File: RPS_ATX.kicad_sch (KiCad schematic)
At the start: 35 parts, among them J1 Fan_in, J10 CTRL, J13 Fan_out, J4 17.5V, J5 PS_OUT-, J6 PS_OUT+, J7 RPS_OUT-, J8 MEAS, J9 RPS_OUT+, Q3 AO3400A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

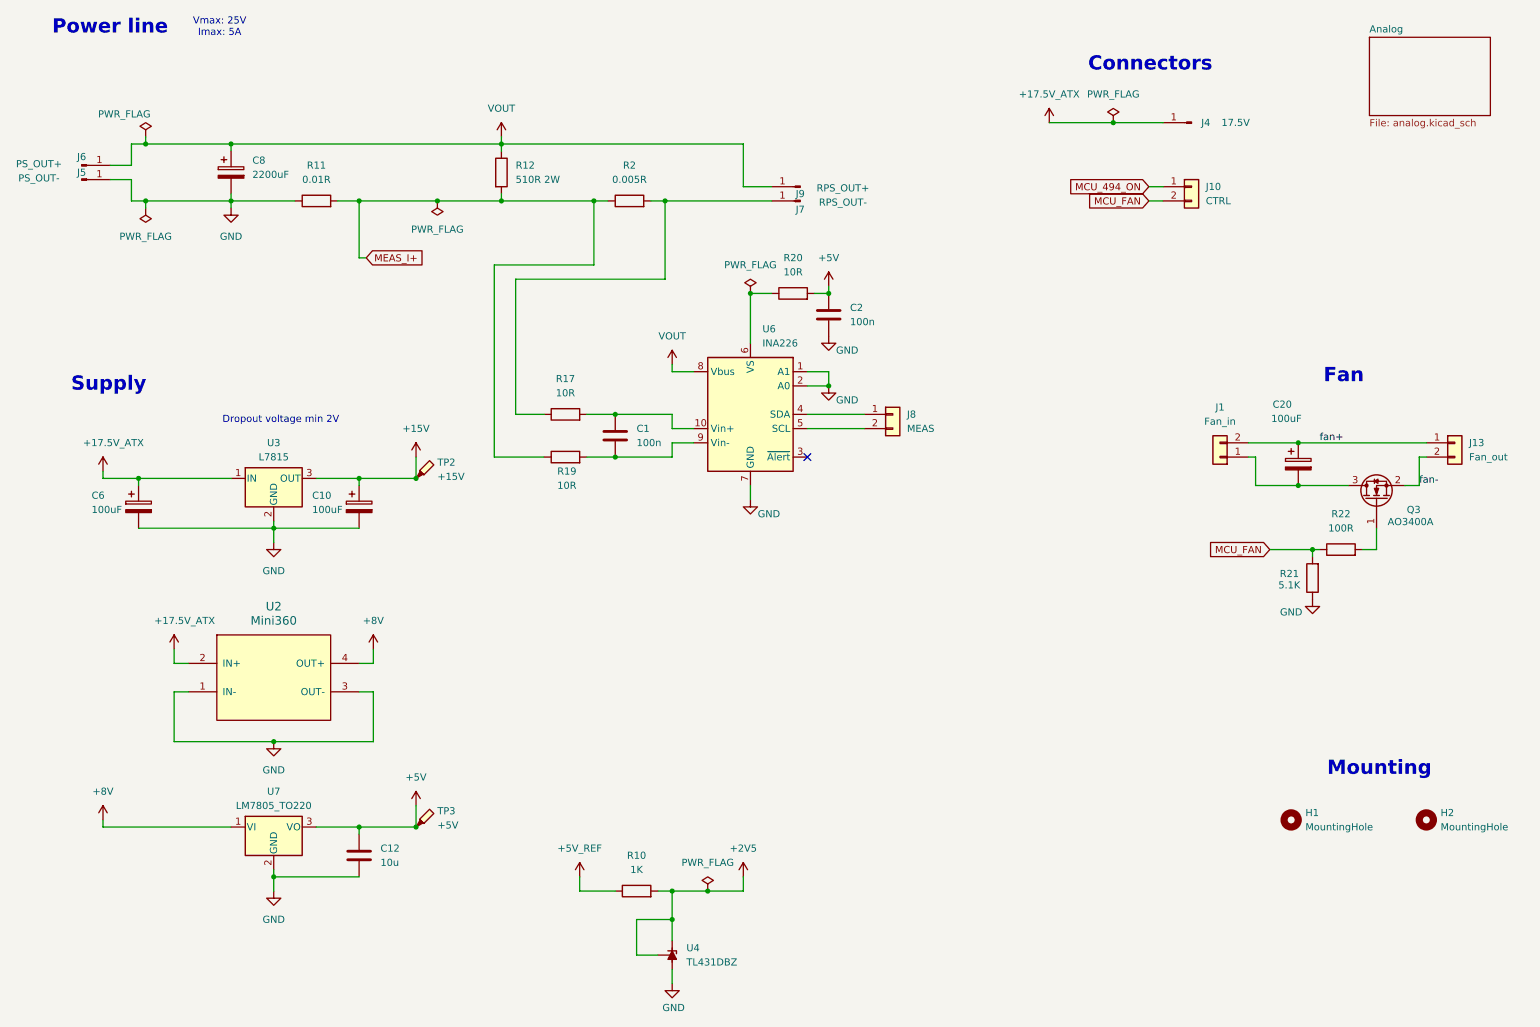
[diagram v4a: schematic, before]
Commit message: lm358 as U and I meas
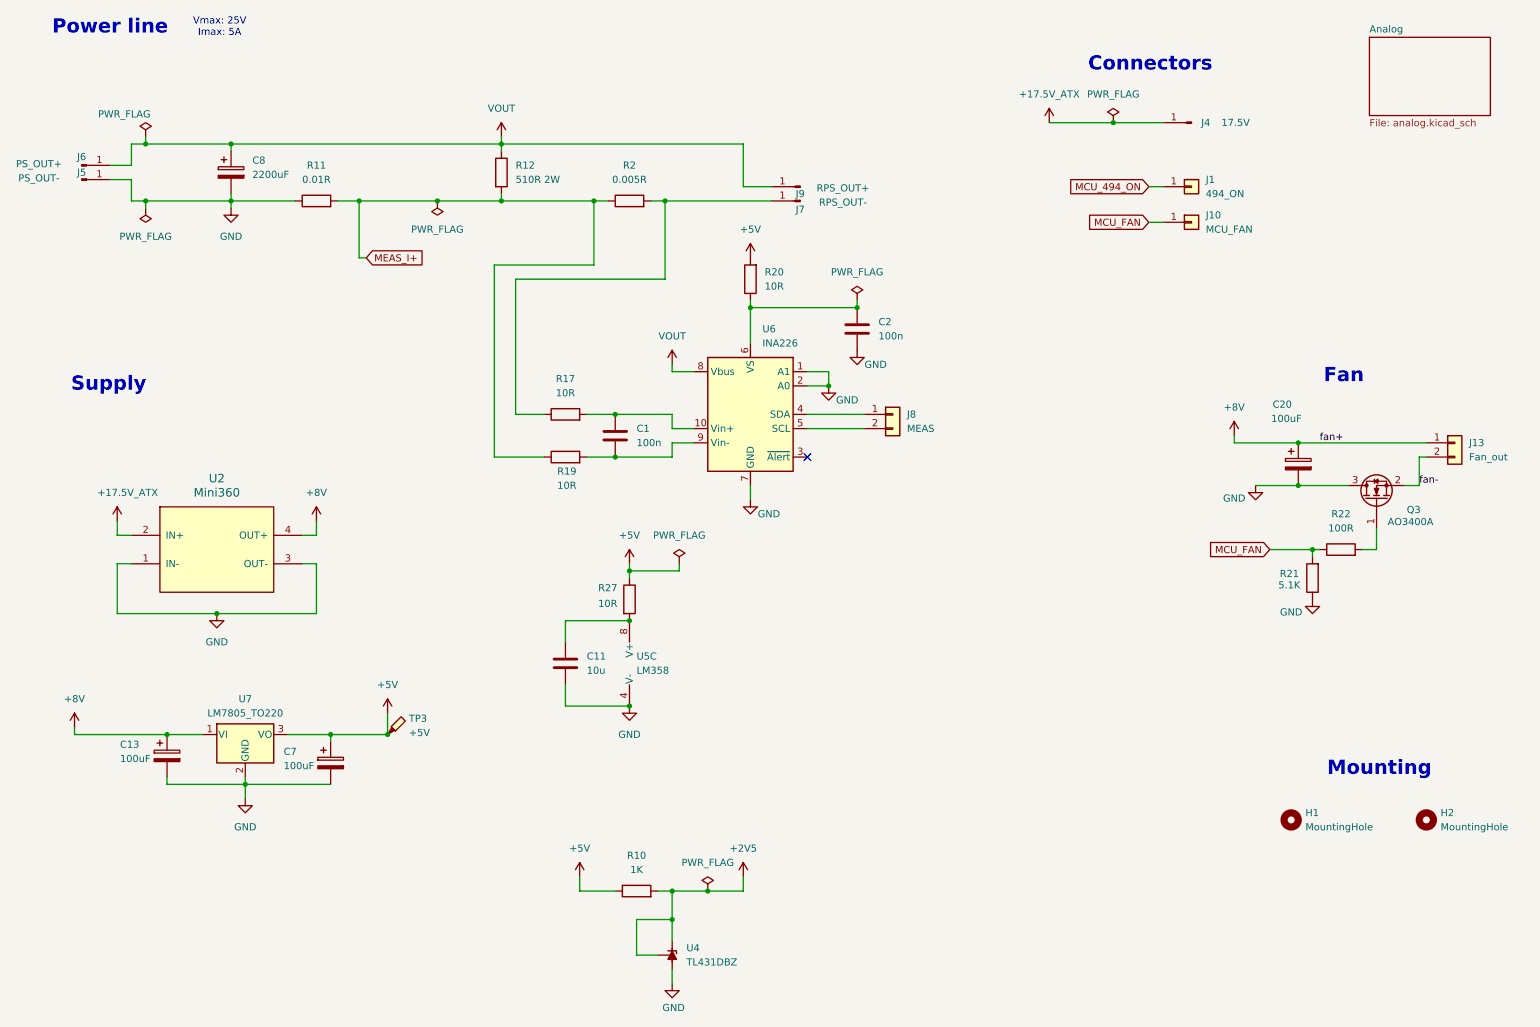
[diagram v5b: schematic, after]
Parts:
- removed C10, C6: 100uF, Capacitor_SMD:CP_Elec_6.3x5.4_Nichicon, symbol Device:C_Polarized
- removed C12: 10u, Capacitor_SMD:C_1206_3216Metric_Pad1.33x1.80mm_HandSolder, symbol Device:C
- removed J1: Fan_in, Connector_PinHeader_2.54mm:PinHeader_1x02_P2.54mm_Vertical, symbol Connector_Generic:Conn_01x02
- removed J10: CTRL, Connector_PinHeader_2.54mm:PinHeader_1x02_P2.54mm_Vertical, symbol Connector_Generic:Conn_01x02
- removed TP2: +15V, TestPoint:TestPoint_Pad_D2.0mm, symbol Connector:TestPoint_Probe
- removed U3: L7815, Package_TO_SOT_THT:TO-220-3_Vertical, symbol Regulator_Linear:L7815
- added C11: 10u, Capacitor_SMD:C_1206_3216Metric_Pad1.33x1.80mm_HandSolder, symbol Device:C
- added C13, C7: 100uF, Capacitor_SMD:CP_Elec_6.3x5.4_Nichicon, symbol Device:C_Polarized
- added J1: 494_ON, Connector_PinHeader_2.54mm:PinHeader_1x01_P2.54mm_Vertical, symbol Connector_Generic:Conn_01x01
- added J10: MCU_FAN, Connector_PinHeader_2.54mm:PinHeader_1x01_P2.54mm_Vertical, symbol Connector_Generic:Conn_01x01
- added R27: 10R, Resistor_SMD:R_1206_3216Metric_Pad1.30x1.75mm_HandSolder, symbol Device:R
- added U5: LM358, Package_SO:SOIC-8_3.9x4.9mm_P1.27mm, symbol Amplifier_Operational:LM358
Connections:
- net +5V_REF is gone; now on net +5V: R10.1
- net fan+ is gone; now on net +8V: C20.1, J13.1 (Pin_1)
- net +5V: now also C7.1, R27.1; no longer C2.1
- net +8V: now also C13.1
- net GND: now also C20.2, Q3.3 (D), C11.2, C13.2, C7.2, U5.4 (V-)
- net MCU_494_ON: now also J1.1 (Pin_1)
- net MCU_FAN: now also J10.1 (Pin_1)
- net at R20.1, U6.6 (VS): now also C2.1
- new net: C11.1, R27.2, U5.8 (V+)
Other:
- note removed: "Dropout voltage min 2V"
- moved on the sheet: C2, R20, TP3, U2, U7

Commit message: added gnd vias, need to isolate power and signal GND
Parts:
- J13: value Fan_out -> FAN_OUT
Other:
- moved on the sheet: J9
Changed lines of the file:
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@@
 	(wire
 		(pts
-			(xy 99.06 39.37) (xy 142.24 39.37)
+			(xy 99.06 39.37) (xy 147.32 39.37)
 		)
 		(stroke
@@
 	(wire
 		(pts
-			(xy 142.24 39.37) (xy 142.24 46.99)
-		)
-		(stroke
-			(width 0)
-			(type default)
-		)
-	)
-	(wire
-		(pts
 			(xy 29.21 43.18) (xy 33.02 43.18)
 		)
@@
 	(wire
 		(pts
-			(xy 142.24 46.99) (xy 147.32 46.99)
-		)
-		(stroke
-			(width 0)
-			(type default)
-		)
-	)
-	(wire
-		(pts
 			(xy 129.54 92.71) (xy 133.35 92.71)
 		)
@@
 			)
 		)
-		(property "Value" "Fan_out"
+		(property "Value" "FAN_OUT"
 			(at 271.78 95.2499 0)
 			(effects
@@
 	(symbol
 		(lib_id "Connector:Conn_01x01_Pin")
-		(at 152.4 46.99 180)
+		(at 152.4 39.37 180)
 		(unit 1)
 		(exclude_from_sim no)
@@
 		(dnp no)
 		(property "Reference" "J9"
-			(at 152.4 48.26 0)
+			(at 152.654 36.83 0)
 			(effects
 				(font
@@
 		)
 		(property "Value" "RPS_OUT+"
-			(at 160.02 47.244 0)
+			(at 159.512 39.37 0)
 			(effects
 				(font
@@
 		)
 		(property "Footprint" "Connector_Wire:SolderWire-2sqmm_1x01_D2mm_OD3.9mm"
-			(at 152.4 46.99 0)
+			(at 152.4 39.37 0)
 			(effects
 				(font
@@
 		)
 		(property "Datasheet" "~"
-			(at 152.4 46.99 0)
+			(at 152.4 39.37 0)
 			(effects
 				(font
@@
 		)
 		(property "Description" "Generic connector, single row, 01x01, script generated"
-			(at 152.4 46.99 0)
+			(at 152.4 39.37 0)
 			(effects
 				(font

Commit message: kind of ready
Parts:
- removed J4: 17.5V, Connector_PinHeader_2.54mm:PinHeader_1x01_P2.54mm_Vertical, symbol Connector:Conn_01x01_Pin
- added J11: PW_IN, Connector_PinHeader_2.54mm:PinHeader_1x02_P2.54mm_Vertical, symbol Connector_Generic:Conn_01x02
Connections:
- net +17.5V_ATX: now also J11.1 (Pin_1)
- net GND: now also J11.2 (Pin_2)
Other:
- moved on the sheet: J1, J10, R27
